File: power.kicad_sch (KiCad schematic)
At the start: 33 parts, among them J1 Conn_01x02_Pin, U1 NS32201, U2 LM3671, U3 NS32016, U4 NS32082, U5 NS32202, U6 74LS08, Y1 12.00000MHz

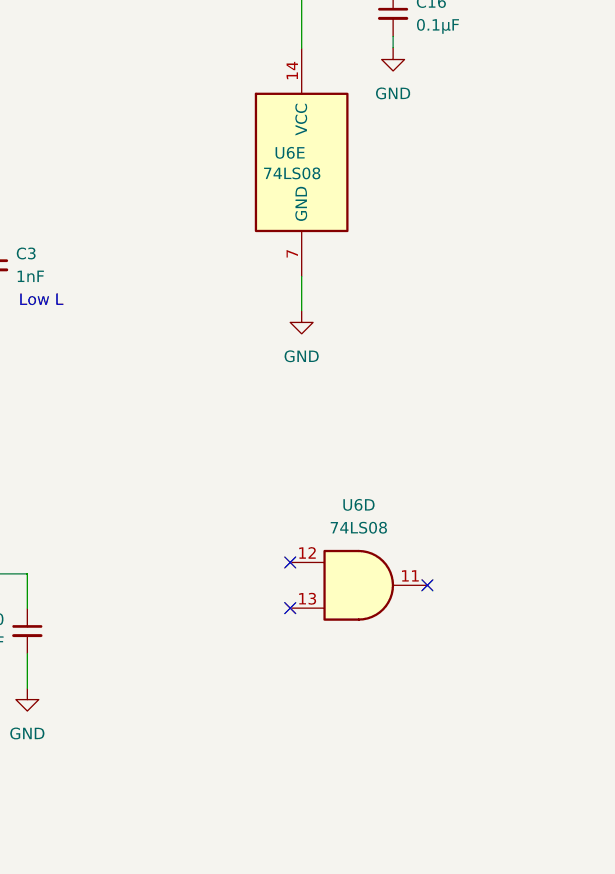
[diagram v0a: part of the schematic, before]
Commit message: add ICU int ack decoding
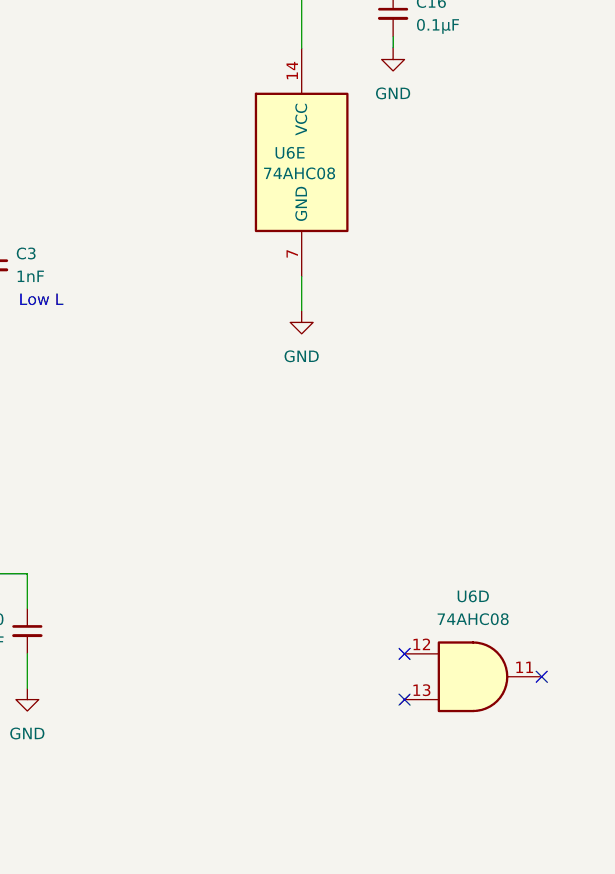
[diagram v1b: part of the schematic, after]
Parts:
- U6: value 74LS08 -> 74AHC08
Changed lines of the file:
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@@
 	)
 	(no_connect
-		(at 213.36 158.75)
+		(at 226.06 173.99)
 	)
 	(no_connect
@@
 	)
 	(no_connect
-		(at 213.36 163.83)
+		(at 226.06 168.91)
 	)
 	(no_connect
-		(at 228.6 161.29)
+		(at 241.3 171.45)
 	)
 	(wire
@@
 			)
 		)
-		(property "Value" "74LS08"
+		(property "Value" "74AHC08"
 			(at 210.312 115.57 0)
 			(effects
@@
 	)
 	(symbol
-		(lib_id "74xx:74LS08")
-		(at 220.98 161.29 0)
-		(unit 4)
-		(exclude_from_sim no)
-		(in_bom yes)
-		(on_board yes)
-		(dnp no)
-		(fields_autoplaced yes)
-		(property "Reference" "U6"
-			(at 220.9717 152.4 0)
-			(effects
-				(font
-					(size 1.27 1.27)
-				)
-			)
-		)
-		(property "Value" "74LS08"
-			(at 220.9717 154.94 0)
-			(effects
-				(font
-					(size 1.27 1.27)
-				)
-			)
-		)
-		(property "Footprint" "Package_SO:TSSOP-14_4.4x5mm_P0.65mm"
-			(at 220.98 161.29 0)
-			(effects
-				(font
-					(size 1.27 1.27)
-				)
-				(hide yes)
-			)
-		)
-		(property "Datasheet" "http://www.ti.com/lit/gpn/sn74LS08"
-			(at 220.98 161.29 0)
-			(effects
-				(font
-					(size 1.27 1.27)
-				)
-				(hide yes)
-			)
-		)
-		(property "Description" "Quad And2"
-			(at 220.98 161.29 0)
-			(effects
-				(font
-					(size 1.27 1.27)
-				)
-				(hide yes)
-			)
-		)
-		(pin "1"
-		)
-		(pin "9"
-		)
-		(pin "4"
-		)
-		(pin "3"
-		)
-		(pin "2"
-		)
-		(pin "8"
-		)
-		(pin "5"
-		)
-		(pin "6"
-		)
-		(pin "10"
-		)
-		(pin "13"
-		)
-		(pin "7"
-		)
-		(pin "14"
-		)
-		(pin "12"
-		)
-		(pin "11"
-		)
-		(instances
-			(project ""
-				(path "/54787df0-1b8c-465f-acae-f55ec7f02da3/c6a0d4a9-2340-4a27-802f-10b03153dcd5"
-					(reference "U6")
-					(unit 4)
-				)
-			)
-		)
-	)
-	(symbol
 		(lib_id "power:GND")
 		(at 40.64 111.76 0)
@@
 				)
 			)
+		)
+	)
+	(symbol
+		(lib_id "74xx:74LS08")
+		(at 233.68 171.45 0)
+		(unit 4)
+		(exclude_from_sim no)
+		(in_bom yes)
+		(on_board yes)
+		(dnp no)
+		(fields_autoplaced yes)
+		(property "Reference" "U6"
+			(at 233.6717 162.56 0)
+			(effects
+				(font
+					(size 1.27 1.27)
+				)
+			)
+		)
+		(property "Value" "74AHC08"
+			(at 233.6717 165.1 0)
+			(effects
+				(font
+					(size 1.27 1.27)
+				)
+			)
+		)
+		(property "Footprint" "Package_SO:TSSOP-14_4.4x5mm_P0.65mm"
+			(at 233.68 171.45 0)
+			(effects
+				(font
+					(size 1.27 1.27)
+				)
+				(hide yes)
+			)
+		)
+		(property "Datasheet" "http://www.ti.com/lit/gpn/sn74LS08"
+			(at 233.68 171.45 0)
+			(effects
+				(font
+					(size 1.27 1.27)
+				)
+				(hide yes)
+			)
+		)
+		(property "Description" "Quad And2"
+			(at 233.68 171.45 0)
+			(effects
+				(font
+					(size 1.27 1.27)
+				)
+				(hide yes)
+			)
+		)
+		(pin "1"
+		)
+		(pin "9"
+		)
+		(pin "4"
+		)
+		(pin "3"
+		)
+		(pin "2"
+		)
+		(pin "8"
+		)
+		(pin "5"
+		)
+		(pin "6"
+		)
+		(pin "10"
+		)
+		(pin "13"
+		)
+		(pin "7"
+		)
+		(pin "14"
+		)
+		(pin "12"
+		)
+		(pin "11"
+		)
+		(instances
+			(project "ns32k"
+				(path "/54787df0-1b8c-465f-acae-f55ec7f02da3/c6a0d4a9-2340-4a27-802f-10b03153dcd5"
+					(reference "U6")
+					(unit 4)
+				)
+			)

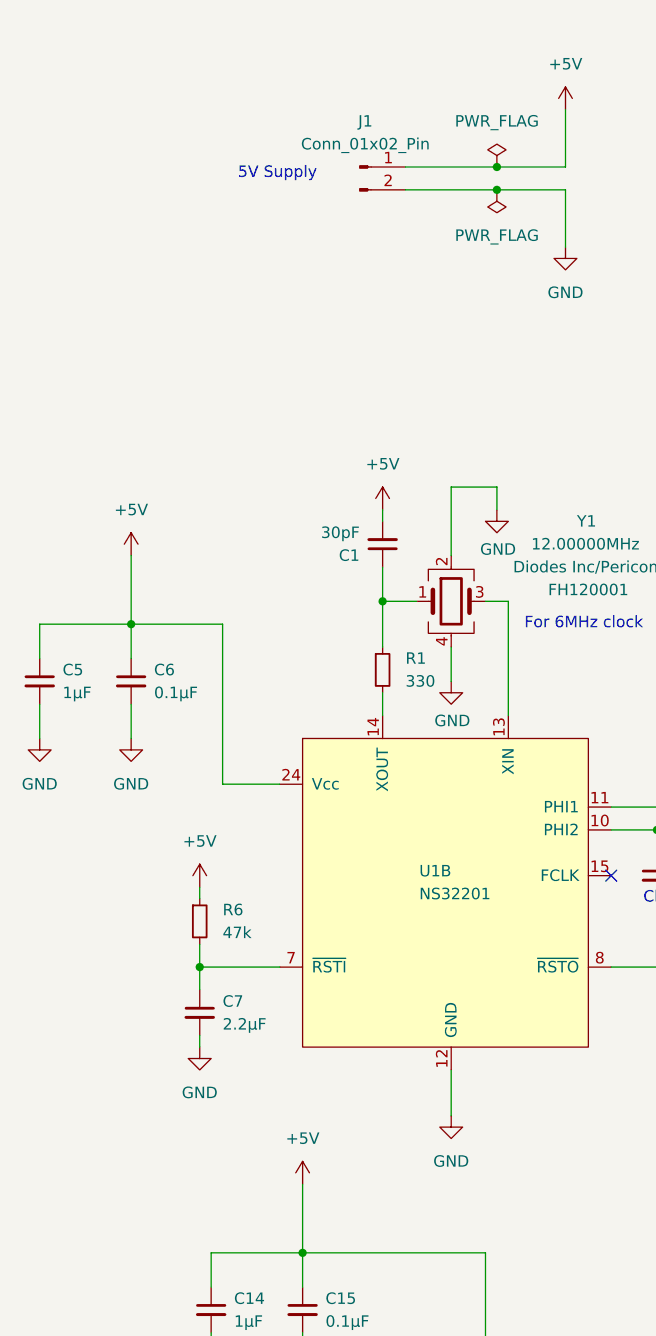
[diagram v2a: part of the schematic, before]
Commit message: add reset button
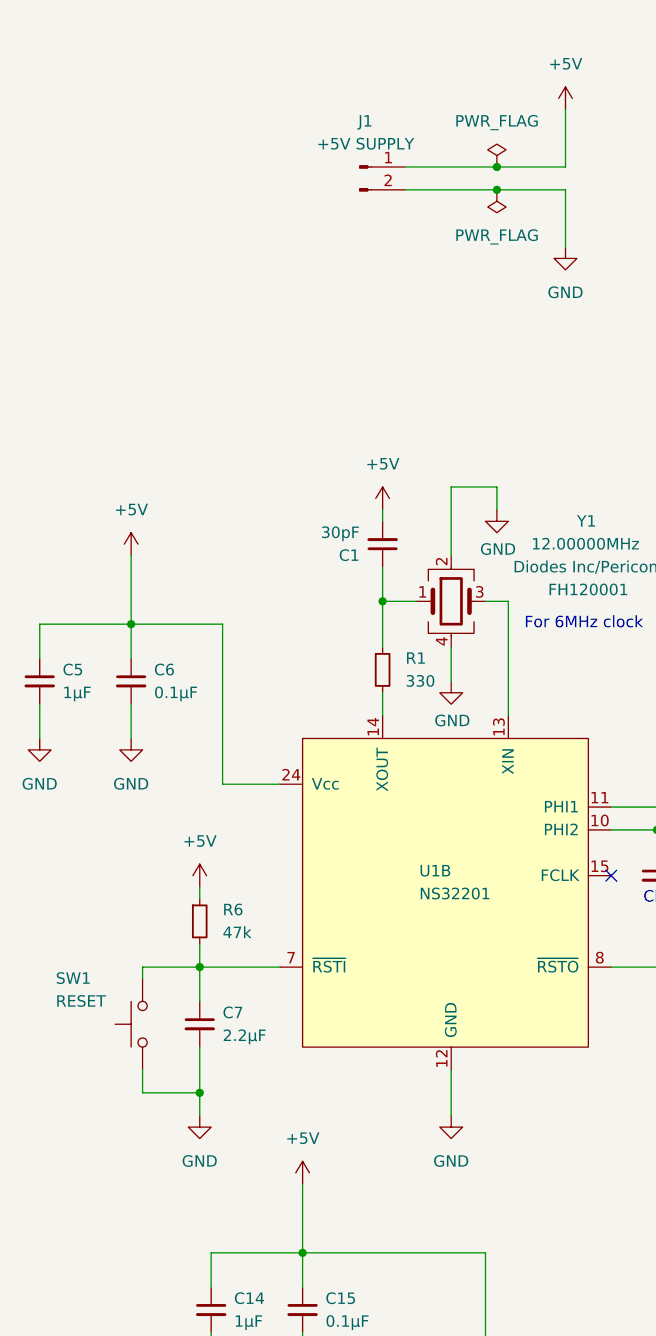
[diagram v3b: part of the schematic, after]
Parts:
- added SW1: RESET, Button_Switch_SMD:SW_SPST_CK_RS282G05A3, symbol Switch:SW_Push
- J1: value Conn_01x02_Pin -> +5V SUPPLY
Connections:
- net GND: now also SW1.2
- net at C7.1, R6.2, U1.7 (~{RSTI}): now also SW1.1
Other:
- note removed: "5V Supply"
- moved on the sheet: C7
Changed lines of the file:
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@@
 	)
 	(junction
+		(at 48.26 151.13)
+		(diameter 0)
+		(color 0 0 0 0)
+	)
+	(junction
 		(at 105.41 119.38)
 		(diameter 0)
@@
 	(wire
 		(pts
-			(xy 48.26 144.78) (xy 48.26 146.05)
+			(xy 48.26 146.05) (xy 48.26 151.13)
 		)
 		(stroke
@@
 	(wire
 		(pts
+			(xy 48.26 151.13) (xy 48.26 153.67)
+		)
+		(stroke
+			(width 0)
+			(type default)
+		)
+	)
+	(wire
+		(pts
 			(xy 180.34 119.38) (xy 170.18 119.38)
 		)
@@
 	(wire
 		(pts
-			(xy 48.26 137.16) (xy 48.26 139.7)
+			(xy 48.26 137.16) (xy 48.26 140.97)
 		)
 		(stroke
@@
 	(wire
 		(pts
+			(xy 41.91 137.16) (xy 41.91 138.43)
+		)
+		(stroke
+			(width 0)
+			(type default)
+		)
+	)
+	(wire
+		(pts
 			(xy 238.76 57.15) (xy 238.76 58.42)
 		)
@@
 	(wire
 		(pts
+			(xy 41.91 148.59) (xy 41.91 151.13)
+		)
+		(stroke
+			(width 0)
+			(type default)
+		)
+	)
+	(wire
+		(pts
 			(xy 40.64 99.06) (xy 40.64 102.87)
 		)
@@
 	(wire
 		(pts
+			(xy 41.91 151.13) (xy 48.26 151.13)
+		)
+		(stroke
+			(width 0)
+			(type default)
+		)
+	)
+	(wire
+		(pts
 			(xy 152.4 139.7) (xy 154.94 139.7)
 		)
@@
 	(wire
 		(pts
+			(xy 41.91 137.16) (xy 48.26 137.16)
+		)
+		(stroke
+			(width 0)
+			(type default)
+		)
+	)
+	(wire
+		(pts
 			(xy 238.76 43.18) (xy 238.76 40.64)
 		)
@@
 		)
 	)
-	(text "5V Supply"
-		(exclude_from_sim no)
-		(at 56.896 49.022 0)
-		(effects
-			(font
-				(size 1.27 1.27)
-			)
-		)
-	)
 	(text "Low L"
 		(exclude_from_sim no)
@@
 	)
 	(symbol
+		(lib_id "Switch:SW_Push")
+		(at 41.91 143.51 90)
+		(mirror x)
+		(unit 1)
+		(exclude_from_sim no)
+		(in_bom yes)
+		(on_board yes)
+		(dnp no)
+		(property "Reference" "SW1"
+			(at 32.258 138.43 90)
+			(effects
+				(font
+					(size 1.27 1.27)
+				)
+				(justify right)
+			)
+		)
+		(property "Value" "RESET"
+			(at 32.258 140.97 90)
+			(effects
+				(font
+					(size 1.27 1.27)
+				)
+				(justify right)
+			)
+		)
+		(property "Footprint" "Button_Switch_SMD:SW_SPST_CK_RS282G05A3"
+			(at 36.83 143.51 0)
+			(effects
+				(font
+					(size 1.27 1.27)
+				)
+				(hide yes)
+			)
+		)
+		(property "Datasheet" "~"
+			(at 36.83 143.51 0)
+			(effects
+				(font
+					(size 1.27 1.27)
+				)
+				(hide yes)
+			)
+		)
+		(property "Description" "Push button switch, generic, two pins"
+			(at 41.91 143.51 0)
+			(effects
+				(font
+					(size 1.27 1.27)
+				)
+				(hide yes)
+			)
+		)
+		(pin "2"
+		)
+		(pin "1"
+		)
+		(instances
+			(project ""
+				(path "/54787df0-1b8c-465f-acae-f55ec7f02da3/c6a0d4a9-2340-4a27-802f-10b03153dcd5"
+					(reference "SW1")
+					(unit 1)
+				)
+			)
+		)
+	)
+	(symbol
 		(lib_id "Device:C_Small")
 		(at 173.99 166.37 0)
@@
 	(symbol
 		(lib_id "Device:C_Small")
-		(at 48.26 142.24 0)
+		(at 48.26 143.51 0)
 		(unit 1)
 		(exclude_from_sim no)
@@
 		(fields_autoplaced yes)
 		(property "Reference" "C7"
-			(at 50.8 140.9762 0)
+			(at 50.8 142.2462 0)
 			(effects
 				(font
@@
 		)
 		(property "Value" "2.2µF"
-			(at 50.8 143.5162 0)
+			(at 50.8 144.7862 0)
 			(effects
 				(font
@@
 		)
 		(property "Footprint" "Capacitor_SMD:C_0603_1608Metric"
-			(at 48.26 142.24 0)
+			(at 48.26 143.51 0)
 			(effects
 				(font
@@
 		)
 		(property "Datasheet" "~"
-			(at 48.26 142.24 0)
+			(at 48.26 143.51 0)
 			(effects
 				(font
@@
 		)
 		(property "Description" "Unpolarized capacitor, small symbol"
-			(at 48.26 142.24 0)
+			(at 48.26 143.51 0)
 			(effects
 				(font
@@
 			)
 		)
-		(property "Value" "Conn_01x02_Pin"
+		(property "Value" "+5V SUPPLY"
 			(at 66.675 45.72 0)
 			(effects
@@
 	(symbol
 		(lib_id "power:GND")
-		(at 48.26 146.05 0)
+		(at 48.26 153.67 0)
 		(unit 1)
 		(exclude_from_sim no)
@@
 		(fields_autoplaced yes)
 		(property "Reference" "#PWR082"
-			(at 48.26 152.4 0)
+			(at 48.26 160.02 0)
 			(effects
 				(font
@@
 		)
 		(property "Value" "GND"
-			(at 48.26 151.13 0)
+			(at 48.26 158.75 0)
 			(effects
 				(font
@@
 		)
 		(property "Footprint" ""
-			(at 48.26 146.05 0)
+			(at 48.26 153.67 0)
 			(effects
 				(font
@@
 		)
 		(property "Datasheet" ""
-			(at 48.26 146.05 0)
+			(at 48.26 153.67 0)
 			(effects
 				(font
@@
 		)
 		(property "Description" "Power symbol creates a global label with name \"GND\" , ground"
-			(at 48.26 146.05 0)
+			(at 48.26 153.67 0)
 			(effects
 				(font

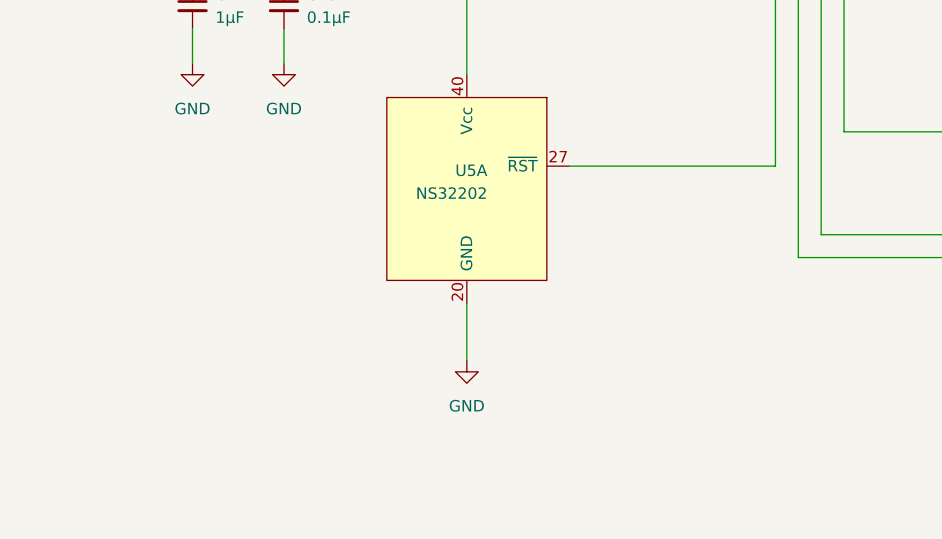
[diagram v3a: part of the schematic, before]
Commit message: fix DRC errors, add RJ45 step model
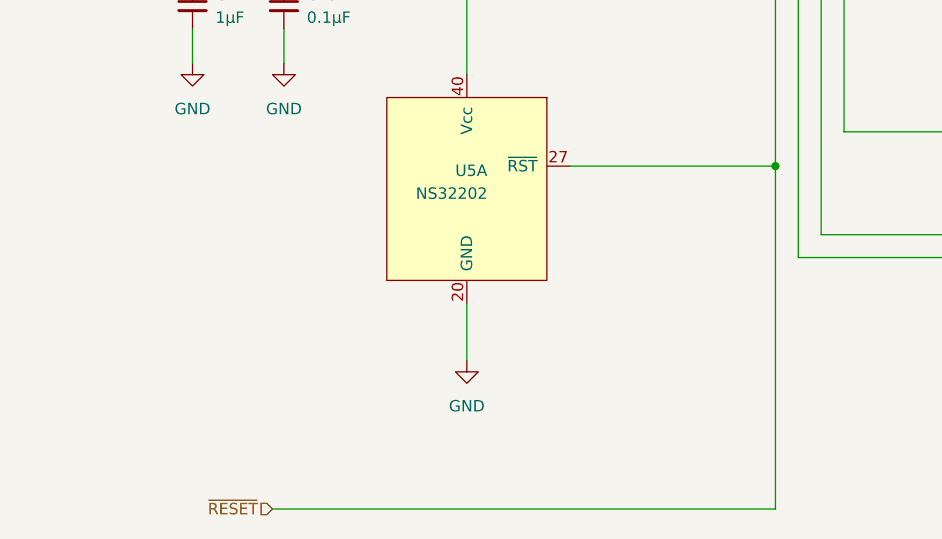
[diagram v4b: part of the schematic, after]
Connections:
- net ~{RESET}: now reaches U3.34 (~{RST}/ABT), U4.34 (~{RST}/ABT), U5.27 (~{RST})
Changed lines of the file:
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@@
 	)
 	(junction
-		(at 81.28 48.26)
+		(at 81.28 50.8)
 		(diameter 0)
 		(color 0 0 0 0)
 	)
 	(junction
-		(at 81.28 50.8)
+		(at 114.3 193.04)
+		(diameter 0)
+		(color 0 0 0 0)
+	)
+	(junction
+		(at 81.28 48.26)
 		(diameter 0)
 		(color 0 0 0 0)
@@
 	(wire
 		(pts
-			(xy 81.28 50.8) (xy 88.9 50.8)
-		)
-		(stroke
-			(width 0)
-			(type default)
-		)
-	)
-	(wire
-		(pts
 			(xy 238.76 40.64) (xy 224.79 40.64)
 		)
@@
 	(wire
 		(pts
+			(xy 58.42 231.14) (xy 114.3 231.14)
+		)
+		(stroke
+			(width 0)
+			(type default)
+		)
+	)
+	(wire
+		(pts
 			(xy 48.26 151.13) (xy 48.26 153.67)
 		)
@@
 	(wire
 		(pts
+			(xy 81.28 50.8) (xy 88.9 50.8)
+		)
+		(stroke
+			(width 0)
+			(type default)
+		)
+	)
+	(wire
+		(pts
 			(xy 59.69 168.91) (xy 80.01 168.91)
 		)
@@
 	(wire
 		(pts
+			(xy 114.3 231.14) (xy 114.3 193.04)
+		)
+		(stroke
+			(width 0)
+			(type default)
+		)
+	)
+	(wire
+		(pts
 			(xy 59.69 168.91) (xy 49.53 168.91)
 		)
@@
 		)
 	)
+	(hierarchical_label "~{RESET}"
+		(shape input)
+		(at 58.42 231.14 180)
+		(fields_autoplaced yes)
+		(effects
+			(font
+				(size 1.27 1.27)
+			)
+			(justify right)
+		)
+	)
 	(symbol
 		(lib_id "74xx:74LS08")
@@
 	)
 	(symbol
-		(lib_id "Device:C_Small")
-		(at 68.58 90.17 0)
-		(mirror x)
+		(lib_id "power:PWR_FLAG")
+		(at 81.28 50.8 180)
 		(unit 1)
 		(exclude_from_sim no)
@@
 		(on_board yes)
 		(dnp no)
-		(property "Reference" "C1"
-			(at 66.04 91.4338 0)
+		(fields_autoplaced yes)
+		(property "Reference" "#FLG02"
+			(at 81.28 52.705 0)
 			(effects
 				(font
 					(size 1.27 1.27)
 				)
-				(justify right)
+				(hide yes)
 			)
 		)
-		(property "Value" "30pF"
-			(at 66.04 88.8938 0)
+		(property "Value" "PWR_FLAG"
+			(at 81.28 55.88 0)
 			(effects
 				(font
 					(size 1.27 1.27)
 				)
-				(justify right)
 			)
 		)
-		(property "Footprint" "Capacitor_SMD:C_0402_1005Metric"
-			(at 68.58 90.17 0)
+		(property "Footprint" ""
+			(at 81.28 50.8 0)
 			(effects
 				(font
@@
 		)
 		(property "Datasheet" "~"
-			(at 68.58 90.17 0)
+			(at 81.28 50.8 0)
 			(effects
 				(font
@@
 			)
 		)
-		(property "Description" "Unpolarized capacitor, small symbol"
-			(at 68.58 90.17 0)
+		(property "Description" "Special symbol for telling ERC where power comes from"
+			(at 81.28 50.8 0)
 			(effects
 				(font
@@
 		(pin "1"
 		)
-		(pin "2"
-		)
 		(instances
-			(project ""
+			(project "ns32k"
 				(path "/54787df0-1b8c-465f-acae-f55ec7f02da3/c6a0d4a9-2340-4a27-802f-10b03153dcd5"
-					(reference "C1")
+					(reference "#FLG02")
 					(unit 1)
 				)
@@
 	)
 	(symbol
-		(lib_id "power:PWR_FLAG")
-		(at 81.28 50.8 180)
+		(lib_id "Device:C_Small")
+		(at 68.58 90.17 0)
+		(mirror x)
 		(unit 1)
 		(exclude_from_sim no)
@@
 		(on_board yes)
 		(dnp no)
-		(fields_autoplaced yes)
-		(property "Reference" "#FLG02"
-			(at 81.28 52.705 0)
+		(property "Reference" "C1"
+			(at 66.04 91.4338 0)
 			(effects
 				(font
 					(size 1.27 1.27)
 				)
-				(hide yes)
+				(justify right)
 			)
 		)
-		(property "Value" "PWR_FLAG"
-			(at 81.28 55.88 0)
+		(property "Value" "30pF"
+			(at 66.04 88.8938 0)
 			(effects
 				(font
 					(size 1.27 1.27)
 				)
+				(justify right)
 			)
 		)
-		(property "Footprint" ""
-			(at 81.28 50.8 0)
+		(property "Footprint" "Capacitor_SMD:C_0402_1005Metric"
+			(at 68.58 90.17 0)
 			(effects
 				(font
@@
 		)
 		(property "Datasheet" "~"
-			(at 81.28 50.8 0)
+			(at 68.58 90.17 0)
 			(effects
 				(font
@@
 			)
 		)
-		(property "Description" "Special symbol for telling ERC where power comes from"
-			(at 81.28 50.8 0)
+		(property "Description" "Unpolarized capacitor, small symbol"
+			(at 68.58 90.17 0)
 			(effects
 				(font
@@
 		(pin "1"
 		)
+		(pin "2"
+		)
 		(instances
 			(project ""
 				(path "/54787df0-1b8c-465f-acae-f55ec7f02da3/c6a0d4a9-2340-4a27-802f-10b03153dcd5"
-					(reference "#FLG02")
+					(reference "C1")
 					(unit 1)
 				)
